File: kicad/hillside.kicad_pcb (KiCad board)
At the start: 2 copper layers, 136.6 x 97.9 mm, 80 parts, among them J1 Haptic, J2 TRRS, J3 Batt_Pos, J4 Batt_GND, K1 SW_Key, K10 SW_Key, K11 SW_Key, K12 SW_Key, K13 SW_Key, K14 SW_Key, K15 SW_Key, K16 SW_Key, K17 SW_Key, K18 SW_Key, K19 SW_Key, K2 SW_Key, K20 SW_Rotary, K21 SW_Key, K22 SW_Key, K23 SW_Key, K24 SW_Key, K3 SW_Key, K4 SW_Key, K5 SW_Key, K6 SW_Key, K7 SW_Key, K8 SW_Key, K9 SW_Key, SW1 Reset, SW2 SW_Power, U1 ProMicro_r

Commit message: Rename to Hillside
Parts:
- H1: footprint redwood:Tenting_Puck -> hillside:Tenting_Puck
- H2: footprint redwood:Pimoroni_Trackball -> hillside:Pimoroni_Trackball
- H3: footprint redwood:Hillside_Scene -> hillside:Hillside_Scene
- J1: footprint redwood:Pimoroni_Haptic -> hillside:Pimoroni_Haptic
- J2: footprint redwood:MJ-4PP-9 -> hillside:MJ-4PP-9
- K1, K10, K11, K12, K13, K14, K15, K16, K17, K18, K19, K2, K21, K22, K23, K24, K3, K4, K5, K6, K7, K8, K9: footprint redwood:pg1350-R -> hillside:pg1350-R
- K20: footprint redwood:pg1350-DR_rotary -> hillside:pg1350-DR_rotary
- U1: footprint redwood:ProMicro_v2 -> hillside:ProMicro_v2
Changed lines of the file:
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@@
     (add_net raw)
   )
-  (module redwood:Hillside_Scene (layer F.Cu)
+  (module hillside:Hillside_Scene (layer F.Cu)
     (at 149.11 121.37)
     (fp_text reference H3 (at 3.25 -14.12) (layer F.Fab)
@@
     )
   )
-  (module redwood:pg1350-R (layer F.Cu)
+  (module hillside:pg1350-R (layer F.Cu)
     (at 215.140348 144.691248 135)
     (fp_text reference K24 (at 0 7 315) (layer F.Fab)
@@
       (net 49 "Net-(D18-Pad2)"))
   )
-  (module redwood:pg1350-R (layer F.Cu)
+  (module hillside:pg1350-R (layer F.Cu)
     (at 207.978277 117.827488 150)
     (fp_text reference K19 (at 0 7 330) (layer F.Fab)
@@
       (net 50 "Net-(D18-Pad1)"))
   )
-  (module redwood:pg1350-R (layer F.Cu)
+  (module hillside:pg1350-R (layer F.Cu)
     (at 199.478277 132.54992 150)
     (fp_text reference K23 (at 0 7 330) (layer F.Fab)
@@
       (net 47 "Net-(D17-Pad2)"))
   )
-  (module redwood:pg1350-R (layer F.Cu)
+  (module hillside:pg1350-R (layer F.Cu)
     (at 181.110001 124.886666 165)
     (fp_text reference K22 (at 0 7 345) (layer F.Fab)
@@
       (net 48 "Net-(D17-Pad1)"))
   )
-  (module redwood:pg1350-R (layer F.Cu)
+  (module hillside:pg1350-R (layer F.Cu)
     (at 161.5 122 180)
     (fp_text reference K21 (at 0 7 180) (layer F.Fab)
@@
       (net 45 "Net-(D16-Pad2)"))
   )
-  (module redwood:pg1350-R (layer F.Cu)
+  (module hillside:pg1350-R (layer F.Cu)
     (at 190 107.5 180)
     (fp_text reference K18 (at 0 7 180) (layer F.Fab)
@@
       (net 43 "Net-(D15-Pad2)"))
   )
-  (module redwood:pg1350-R (layer F.Cu)
+  (module hillside:pg1350-R (layer F.Cu)
     (at 172 105 180)
     (fp_text reference K17 (at 0 7 180) (layer F.Fab)
@@
       (net 44 "Net-(D15-Pad1)"))
   )
-  (module redwood:pg1350-R (layer F.Cu)
+  (module hillside:pg1350-R (layer F.Cu)
     (at 190 90.5 180)
     (fp_text reference K12 (at 0 7 180) (layer F.Fab)
@@
       (net 41 "Net-(D12-Pad2)"))
   )
-  (module redwood:pg1350-R (layer F.Cu)
+  (module hillside:pg1350-R (layer F.Cu)
     (at 172 88 180)
     (fp_text reference K11 (at 0 7 180) (layer F.Fab)
@@
       (net 42 "Net-(D12-Pad1)"))
   )
-  (module redwood:pg1350-R (layer F.Cu)
+  (module hillside:pg1350-R (layer F.Cu)
     (at 190 73.5 180)
     (fp_text reference K6 (at 0 7 180) (layer F.Fab)
@@
       (net 32 "Net-(D9-Pad2)"))
   )
-  (module redwood:pg1350-R (layer F.Cu)
+  (module hillside:pg1350-R (layer F.Cu)
     (at 172 71 180)
     (fp_text reference K5 (at 0 7 180) (layer F.Fab)
@@
       (net 31 "Net-(D9-Pad1)"))
   )
-  (module redwood:pg1350-R (layer F.Cu)
+  (module hillside:pg1350-R (layer F.Cu)
     (at 154 99.5 180)
     (fp_text reference K16 (at 0 7 180) (layer F.Fab)
@@
       (net 37 "Net-(D14-Pad2)"))
   )
-  (module redwood:pg1350-R (layer F.Cu)
+  (module hillside:pg1350-R (layer F.Cu)
     (at 136 106.5 180)
     (fp_text reference K15 (at 0 7 180) (layer F.Fab)
@@
       (net 38 "Net-(D14-Pad1)"))
   )
-  (module redwood:pg1350-R (layer F.Cu)
+  (module hillside:pg1350-R (layer F.Cu)
     (at 154 82.5 180)
     (fp_text reference K10 (at 0 7 180) (layer F.Fab)
@@
       (net 35 "Net-(D11-Pad2)"))
   )
-  (module redwood:pg1350-R (layer F.Cu)
+  (module hillside:pg1350-R (layer F.Cu)
     (at 136 89.5 180)
     (fp_text reference K9 (at 0 7 180) (layer F.Fab)
@@
       (net 36 "Net-(D11-Pad1)"))
   )
-  (module redwood:pg1350-R (layer F.Cu)
+  (module hillside:pg1350-R (layer F.Cu)
     (at 118 118.5 180)
     (fp_text reference K14 (at 0 7 180) (layer F.Fab)
@@
       (net 33 "Net-(D13-Pad2)"))
   )
-  (module redwood:pg1350-R (layer F.Cu)
+  (module hillside:pg1350-R (layer F.Cu)
     (at 100 118.5 180)
     (fp_text reference K13 (at 0 7 180) (layer F.Fab)
@@
       (net 34 "Net-(D13-Pad1)"))
   )
-  (module redwood:pg1350-R (layer F.Cu)
+  (module hillside:pg1350-R (layer F.Cu)
     (at 118 84.5 180)
     (fp_text reference K2 (at 0 7 180) (layer F.Fab)
@@
       (net 28 "Net-(D7-Pad2)"))
   )
-  (module redwood:pg1350-R (layer F.Cu)
+  (module hillside:pg1350-R (layer F.Cu)
     (at 118 101.5 180)
     (fp_text reference K8 (at 0 7 180) (layer F.Fab)
@@
       (net 39 "Net-(D10-Pad2)"))
   )
-  (module redwood:pg1350-R (layer F.Cu)
+  (module hillside:pg1350-R (layer F.Cu)
     (at 100 101.5 180)
     (fp_text reference K7 (at 0 7 180) (layer F.Fab)
@@
       (net 40 "Net-(D10-Pad1)"))
   )
-  (module redwood:pg1350-R (layer F.Cu)
+  (module hillside:pg1350-R (layer F.Cu)
     (at 154 65.5 180)
     (fp_text reference K4 (at 0 7 180) (layer F.Fab)
@@
       (net 30 "Net-(D8-Pad2)"))
   )
-  (module redwood:pg1350-R (layer F.Cu)
+  (module hillside:pg1350-R (layer F.Cu)
     (at 136 72.5 180)
     (fp_text reference K3 (at 0 7 180) (layer F.Fab)
@@
       (net 29 "Net-(D8-Pad1)"))
   )
-  (module redwood:pg1350-R (layer F.Cu)
+  (module hillside:pg1350-R (layer F.Cu)
     (at 100 84.5 180)
     (fp_text reference K1 (at 0 7 180) (layer F.Fab)
@@
     )
   )
-  (module redwood:MJ-4PP-9 (layer F.Cu)
+  (module hillside:MJ-4PP-9 (layer F.Cu)
     (at 214.48 129.36 90)
     (fp_text reference J2 (at -1.99 10.82 270) (layer F.Fab)
@@
     )
   )
-  (module redwood:ProMicro_v2 (layer F.Cu)
+  (module hillside:ProMicro_v2 (layer F.Cu)
     (at 210 86.63)
     (fp_text reference U1 (at 0 -1.63) (layer F.Fab) hide
@@
       (net 52 raw))
   )
-  (module redwood:Tenting_Puck (layer F.Cu)
+  (module hillside:Tenting_Puck (layer F.Cu)
     (at 163.01 81.96)
     (fp_text reference H1 (at 0.01 0.01) (layer Cmts.User) hide
@@
     (pad "" thru_hole circle (at -19.05 0) (size 4.4 4.4) (drill 2.2) (layers *.Cu *.Mask))
   )
-  (module redwood:pg1350-DR_rotary (layer F.Cu)
+  (module hillside:pg1350-DR_rotary (layer F.Cu)
     (at 136 119 180)
     (fp_text reference K20 (at 0.05 -0.5) (layer F.Fab) hide
@@
     (pad "" np_thru_hole circle (at 0 -4.5 180) (size 3.4 3.4) (drill 3.4) (layers *.Cu *.Mask))
   )
-  (module redwood:Pimoroni_Haptic (layer F.Cu)
+  (module hillside:Pimoroni_Haptic (layer F.Cu)
     (at 215.475 93.45)
     (descr "Pimoroni Haptic PIM452 header 2.54mm pitch and one mount point")
@@
     (pad "" thru_hole circle (at 6.75 -8.25) (size 5 5) (drill 2.5) (layers *.Cu *.Mask))
   )
-  (module redwood:Pimoroni_Trackball (layer F.Cu)
+  (module hillside:Pimoroni_Trackball (layer F.Cu)
     (at 212 112.92 180)
     (descr "Through hole header 2.54mm pitch and one of two mount points for Pomoroni Haptic PIM452")

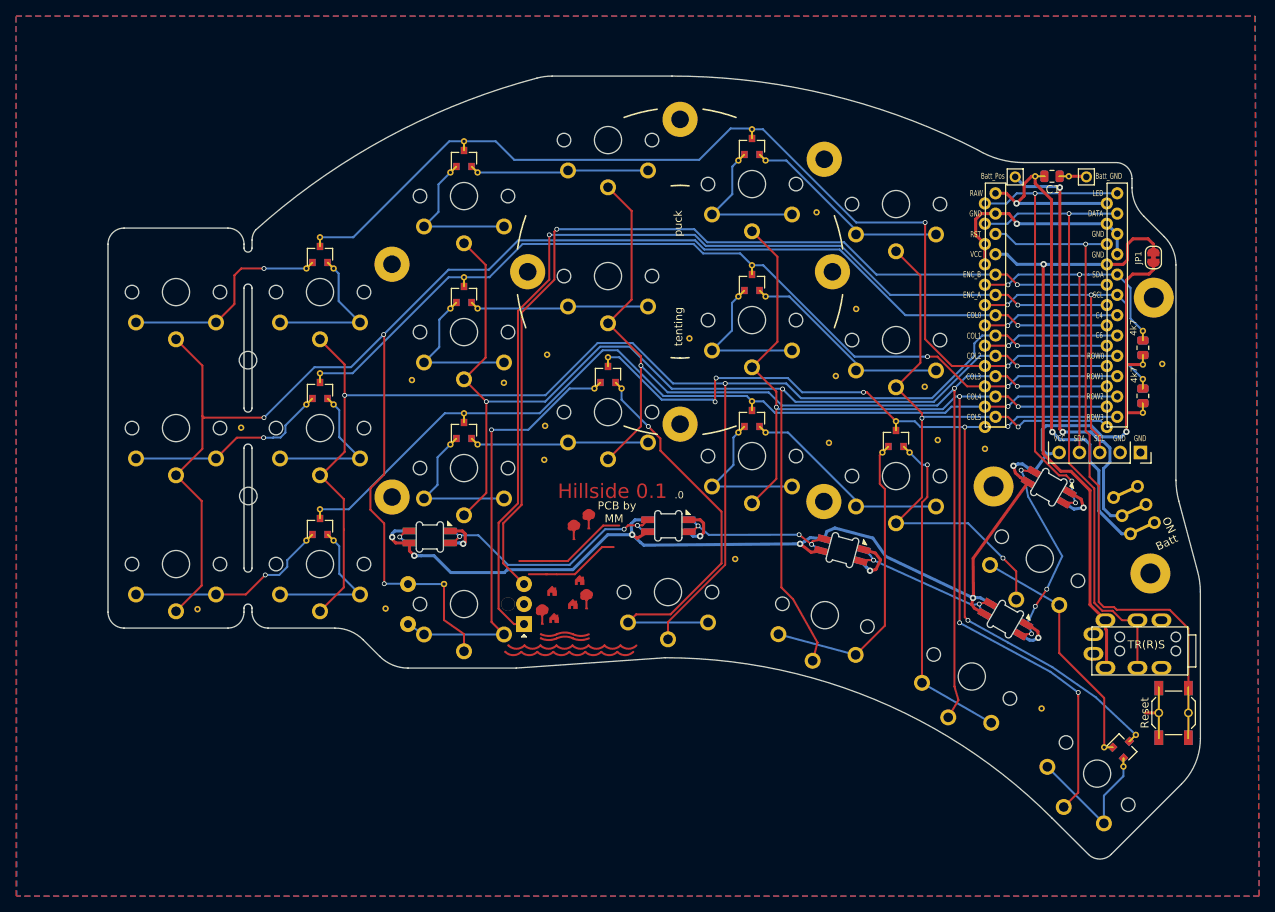
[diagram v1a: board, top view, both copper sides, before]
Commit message: TRRS order has no-connect, cleanup matrix layout
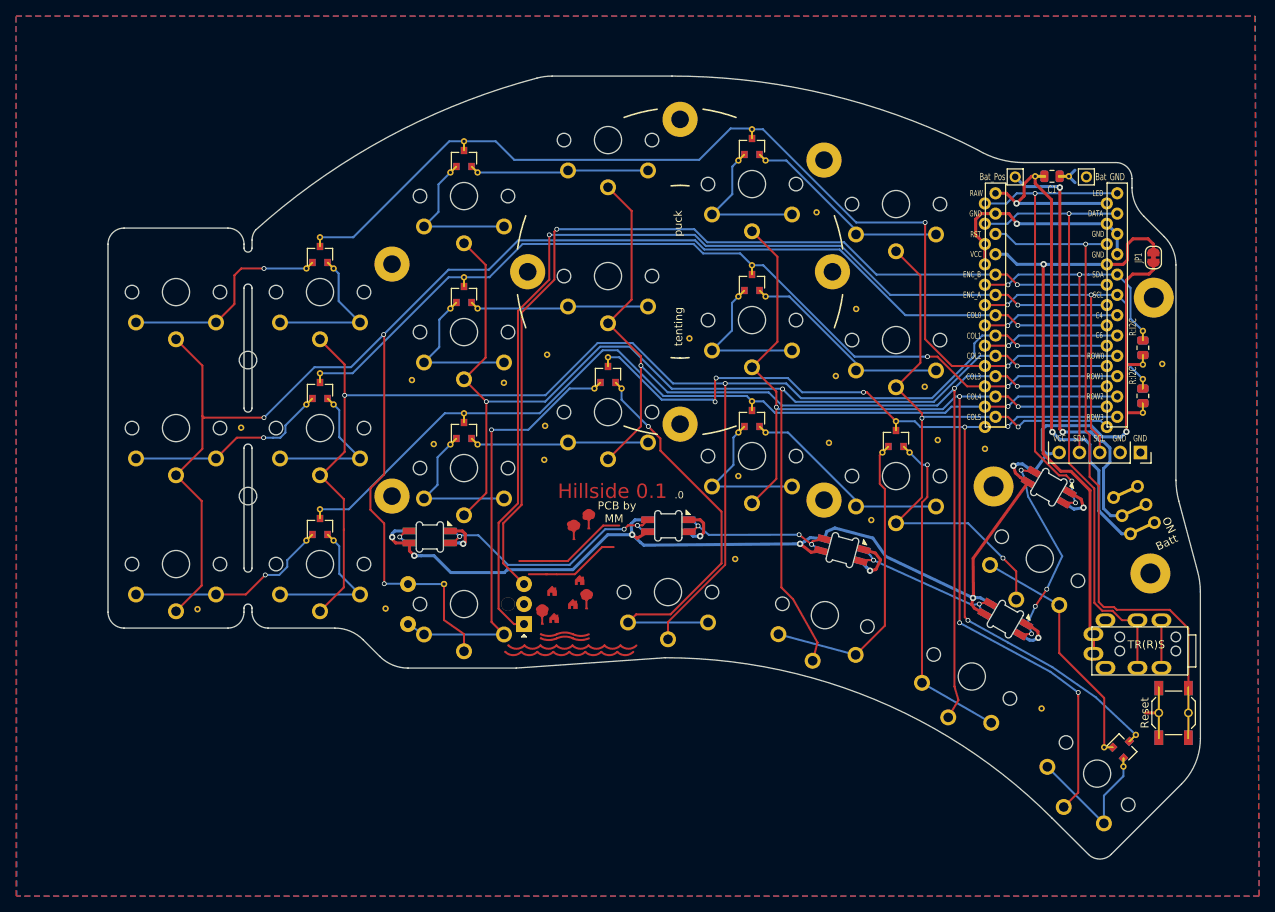
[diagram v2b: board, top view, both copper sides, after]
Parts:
- added V20: Via, ki_syms:VIA-0.8mm, F.Cu at (186.9, 113.0)
- added V21: Via, ki_syms:VIA-0.8mm, F.Cu at (132.2, 103.5)
- added V22: Via, ki_syms:VIA-0.8mm, F.Cu at (170.3, 107.5)
- H4, H5, H8, H9: footprint ki_mount_hole:MountingHole_2.2mm_M2_Pad -> ki_syms:MountingHole_2.2mm_M2_Pad
- H6, H7: footprint ki_mount_hole:MountingHole_2.2mm_M2 -> ki_syms:MountingHole_2.2mm_M2
- J3: value Batt_Pos -> Bat_Pos
- J4: value Batt_GND -> Bat_GND
- JP1: value SolderJumper_2_Bridged -> SolderJumper
- R1, R2: value 4k7 -> R:I2C
- moved H8 0.18 mm to (181.0, 110.5)
- moved H5 0.12 mm to (127.0, 110.0)
- moved H9 0.10 mm to (181.0, 68.0)
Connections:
- J2 pad R2: GND -> Net-(J2-PadR2)
- J2 pad S: GND -> VCC
- J2 pad T: VCC -> GND
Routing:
- net Net-(J2-PadR2): track 0.00 -> 5.95 mm
- net VCC: track 78.8 -> 76.1 mm

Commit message: - project: gerber_hillside output dir
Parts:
- H3: value Scene -> Logo; footprint hillside:Hillside_Scene -> hillside:Hillside_Logo

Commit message: Common symbols/footprints used in hillside_basic
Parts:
- C1: footprint ki_syms:C_0805_2012Metric -> hillside_basic:C_0805_2012Metric
- D1, D2, D3, D4, D5: footprint ki_syms:SK6812-MINI-E -> hillside_basic:SK6812-MINI-E
- D10, D11, D12, D13, D14, D15, D16, D17, D18, D7, D8, D9: footprint ki_syms:SOT-23 -> hillside_basic:SOT-23
- H4, H5, H8, H9: footprint ki_syms:MountingHole_2.2mm_M2_Pad -> hillside_basic:MountingHole_2.2mm_M2_Pad
- H6, H7: footprint ki_syms:MountingHole_2.2mm_M2 -> hillside_basic:MountingHole_2.2mm_M2
- J3, J4: footprint ki_syms:1pin_conn -> hillside_basic:1pin_conn
- JP1: footprint ki_syms:SolderJumper-2_P1.3mm_Bridged_RoundedPad1.0x1.5mm -> hillside_basic:SolderJumper-2_P1.3mm_Bridged_RoundedPad1.0x1.5mm
- R1, R2: footprint ki_syms:R_0805_2012Metric -> hillside_basic:R_0805_2012Metric
- SW1: footprint ki_syms:SW_SPST_SKQG_WithStem -> hillside_basic:SW_SPST_SKQG_WithStem
- SW2: footprint ki_syms:SW_SPDT_JS202011AQN -> hillside_basic:SW_SPDT_JS202011AQN
- V1, V10, V11, V12, V13, V14, V15, V16, V17, V18, V19, V2, V20, V21, V22, V3, V4, V5, V6, V7, V8, V9: footprint ki_syms:VIA-0.8mm -> hillside_basic:VIA-0.8mm

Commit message: - cleanup via name
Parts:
- V1: value V -> Via
